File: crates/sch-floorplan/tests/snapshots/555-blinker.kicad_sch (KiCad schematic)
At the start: 7 parts, among them U1 NE555P

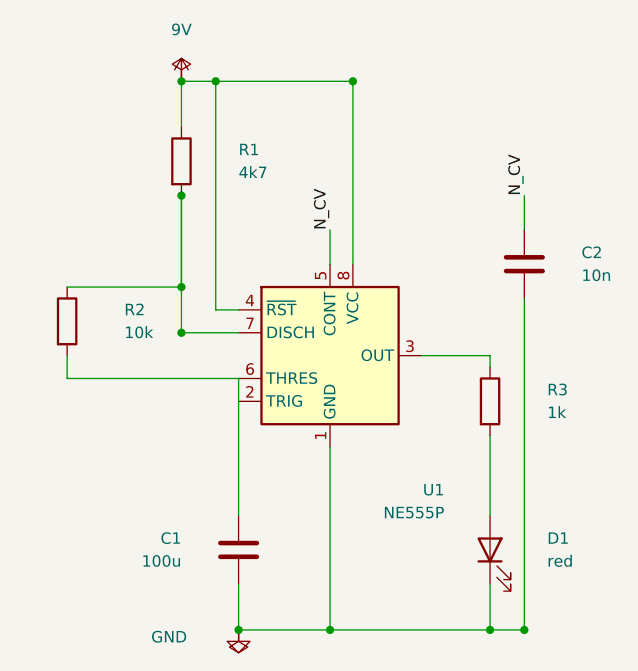
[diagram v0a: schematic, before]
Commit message: sch-doc: pick the smallest standard page from an A5-first ladder
A four-part circuit on A4 is a drawing stranded in one corner of an
empty sheet; the critic scored that a point worse than the snug custom
page it replaced. Starting the ladder at A5 keeps the frame close to
the content while every sheet still lands on a size KiCad and a printer
recognise.

Re-blessed the five snapshots whose critic score held at or above their
pre-change score. grid-demo is left at its baseline: it renders 7 where
it used to render 9.

Claude-Session: https://claude.ai/code/session_01GyGRY43X8yBh8WS1tjEmFz
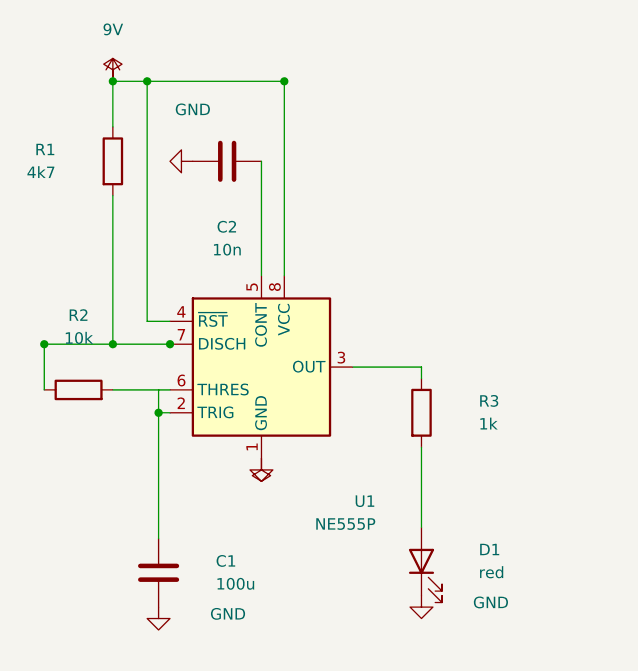
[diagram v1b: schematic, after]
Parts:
- C1, C2, D1, R1, R2, R3, U1: ap_block (none) -> blinker
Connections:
- net N_CV: no longer names the net of C2.1, U1.5 (CONT)
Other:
- moved on the sheet: C1, C2, D1, R1, R2, R3, U1
